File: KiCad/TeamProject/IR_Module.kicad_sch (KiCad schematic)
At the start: 20 parts, among them U1 MCP6294, U4 MCP6294, U4 MCP6546, U6 MCP6294

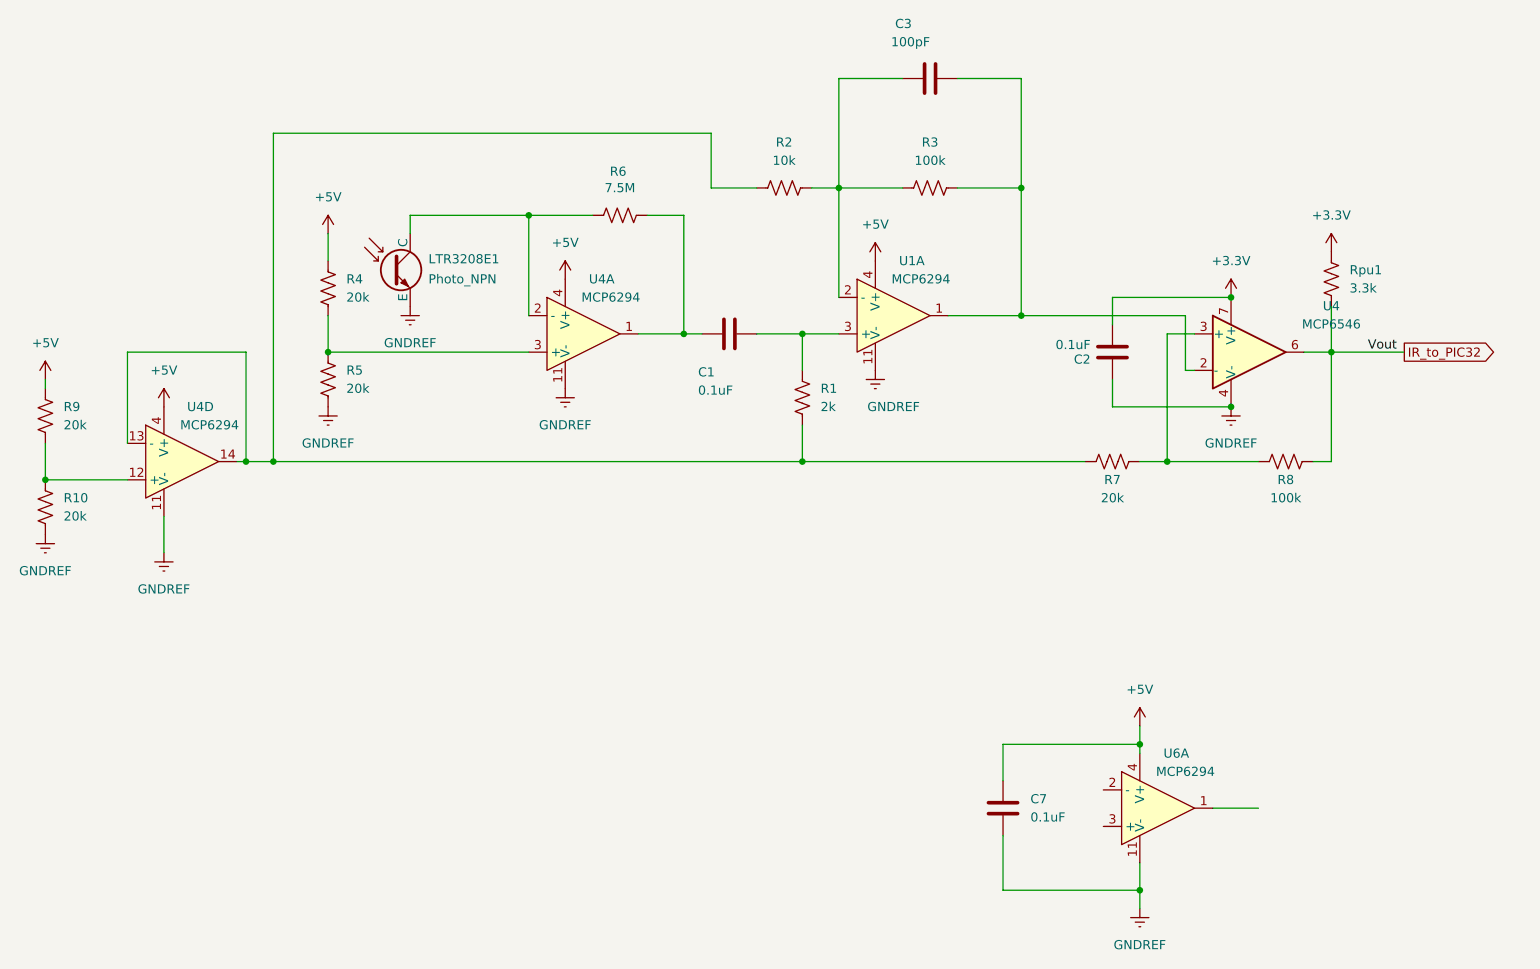
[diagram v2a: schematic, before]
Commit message: Update first-stage amplifier resistor value for IR module
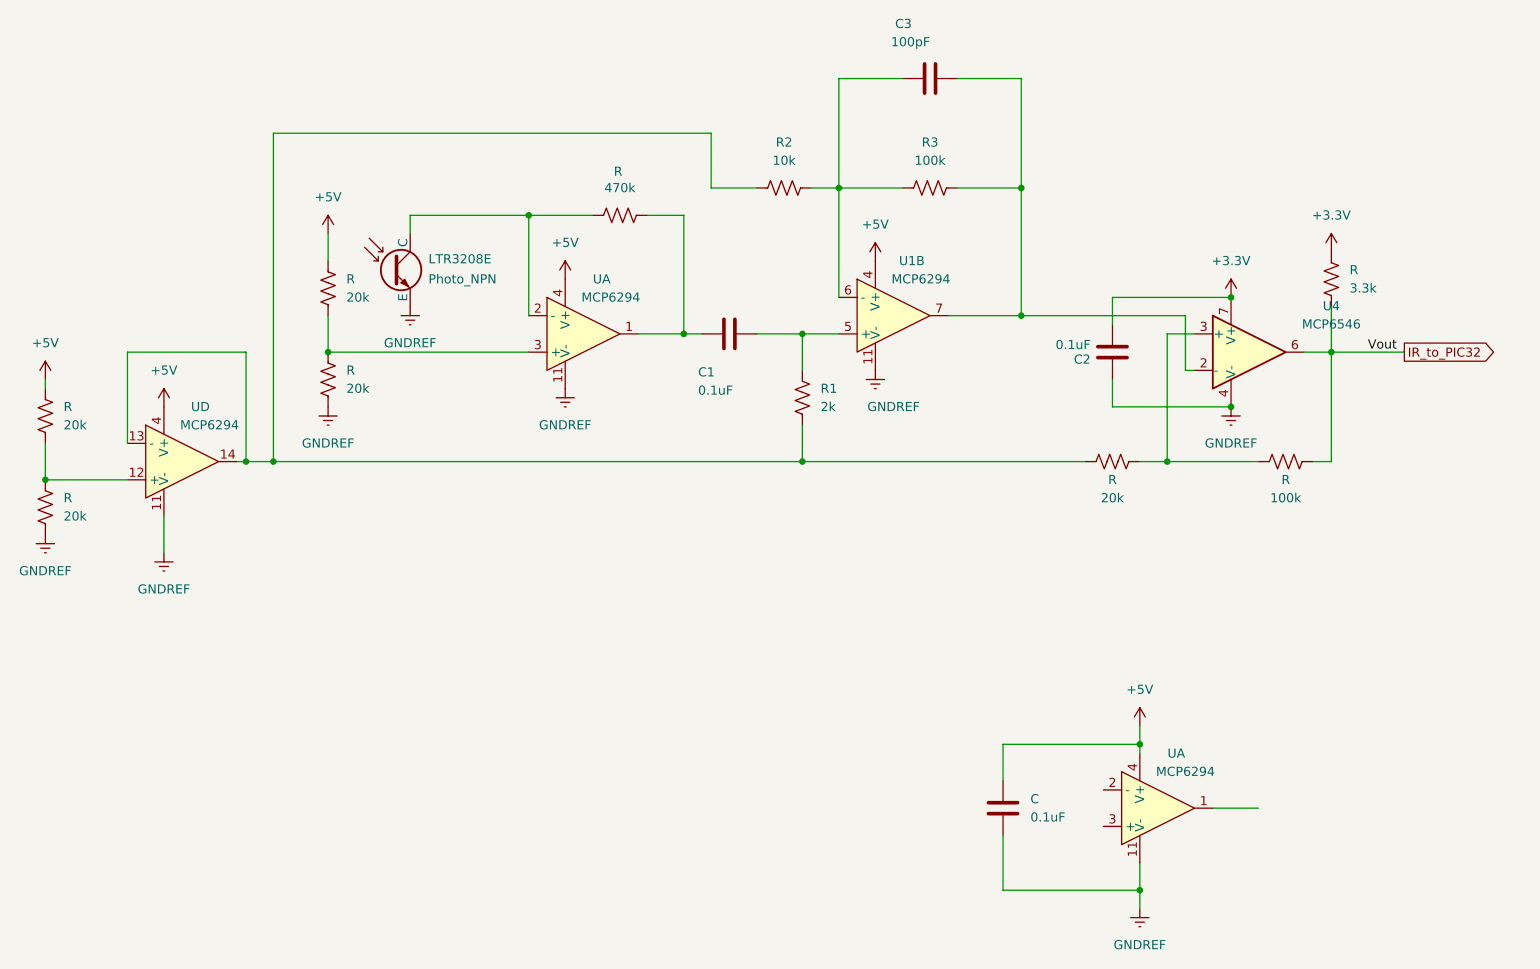
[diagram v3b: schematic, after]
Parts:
- R: renamed from R6; value 7.5M -> 470k
- renumbered C7 to C, LTR3208E1 to LTR3208E, R7 to R, R8 to R, R9 to R, Rpu1 to R, R10 to R, R5 to R, R4 to R, U4 to U, U6 to U
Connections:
- net at C3.1, R3.2, U4.2 (-): now also U1.7; no longer U1.1
- net at C3.2, R2.2, R3.1: now also U1.6 (-); no longer U1.2 (-)
- net at C1.1, R1.2: now also U1.5 (+); no longer U1.3 (+)
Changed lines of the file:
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@@
 		(on_board yes)
 		(dnp no)
-		(property "Reference" "#PWR?"
+		(property "Reference" "#PWR02"
 			(at 166.37 90.17 0)
 			(effects
@@
 		(on_board yes)
 		(dnp no)
-		(property "Reference" "C?"
+		(property "Reference" "C2"
 			(at 196.342 82.296 0)
 			(effects
@@
 		(lib_id "ME218_BaseLib:MCP6294")
 		(at 168.91 76.2 0)
-		(unit 1)
-		(exclude_from_sim no)
-		(in_bom yes)
-		(on_board yes)
-		(dnp no)
-		(property "Reference" "U?"
+		(unit 2)
+		(exclude_from_sim no)
+		(in_bom yes)
+		(on_board yes)
+		(dnp no)
+		(property "Reference" "U1"
 			(at 171.45 68.58 0)
 			(effects
@@
 		(on_board yes)
 		(dnp no)
-		(property "Reference" "R7"
+		(property "Reference" "R"
 			(at 199.39 99.06 90)
 			(effects
@@
 		(dnp no)
 		(fields_autoplaced yes)
-		(property "Reference" "R?"
+		(property "Reference" "R3"
 			(at 173.99 52.07 90)
 			(effects
@@
 		(dnp no)
 		(fields_autoplaced yes)
-		(property "Reference" "R?"
+		(property "Reference" "R1"
 			(at 158.75 86.3599 0)
 			(effects
@@
 		(dnp no)
 		(fields_autoplaced yes)
-		(property "Reference" "#PWR?"
+		(property "Reference" "#PWR03"
 			(at 101.6 81.28 0)
 			(effects
@@
 		(dnp no)
 		(fields_autoplaced yes)
-		(property "Reference" "#PWR09"
+		(property "Reference" "#PWR?"
 			(at 90.17 95.25 0)
 			(effects
@@
 		(on_board yes)
 		(dnp no)
-		(property "Reference" "R8"
+		(property "Reference" "R"
 			(at 223.52 99.06 90)
 			(effects
@@
 		(dnp no)
 		(fields_autoplaced yes)
-		(property "Reference" "R9"
+		(property "Reference" "R"
 			(at 53.34 88.8999 0)
 			(effects
@@
 		(dnp no)
 		(fields_autoplaced yes)
-		(property "Reference" "#PWR?"
+		(property "Reference" "#PWR01"
 			(at 166.37 72.39 0)
 			(effects
@@
 		(on_board yes)
 		(dnp no)
-		(property "Reference" "U?"
+		(property "Reference" "U4"
 			(at 229.87 74.8598 0)
 			(effects
@@
 		(dnp no)
 		(fields_autoplaced yes)
-		(property "Reference" "#PWR029"
+		(property "Reference" "#PWR?"
 			(at 215.9 77.47 0)
 			(effects
@@
 		(dnp no)
 		(fields_autoplaced yes)
-		(property "Reference" "#PWR032"
+		(property "Reference" "#PWR?"
 			(at 67.31 115.57 0)
 			(effects
@@
 		(on_board yes)
 		(dnp no)
-		(property "Reference" "C?"
+		(property "Reference" "C1"
 			(at 144.018 84.074 90)
 			(effects
@@
 		(dnp no)
 		(fields_autoplaced yes)
-		(property "Reference" "#PWR023"
+		(property "Reference" "#PWR?"
 			(at 123.19 74.93 0)
 			(effects
@@
 		(on_board yes)
 		(dnp no)
-		(property "Reference" "C?"
+		(property "Reference" "C3"
 			(at 171.45 35.56 90)
 			(effects
@@
 		(dnp no)
 		(fields_autoplaced yes)
-		(property "Reference" "C7"
+		(property "Reference" "C"
 			(at 187.96 143.5099 0)
 			(effects
@@
 		(dnp no)
 		(fields_autoplaced yes)
-		(property "Reference" "#PWR030"
+		(property "Reference" "#PWR?"
 			(at 215.9 95.25 0)
 			(effects
@@
 		(dnp no)
 		(fields_autoplaced yes)
-		(property "Reference" "#PWR024"
+		(property "Reference" "#PWR?"
 			(at 123.19 92.71 0)
 			(effects
@@
 		(dnp no)
 		(fields_autoplaced yes)
-		(property "Reference" "#PWR021"
+		(property "Reference" "#PWR?"
 			(at 50.8 113.03 0)
 			(effects
@@
 		(dnp no)
 		(fields_autoplaced yes)
-		(property "Reference" "#PWR031"
+		(property "Reference" "#PWR?"
 			(at 67.31 92.71 0)
 			(effects
@@
 		(on_board yes)
 		(dnp no)
-		(property "Reference" "U4"
+		(property "Reference" "U"
 			(at 72.39 88.9 0)
 			(effects
@@
 		(dnp no)
 		(fields_autoplaced yes)
-		(property "Reference" "#PWR020"
+		(property "Reference" "#PWR?"
 			(at 50.8 88.9 0)
 			(effects
@@
 		(dnp no)
 		(fields_autoplaced yes)
-		(property "Reference" "Rpu1"
+		(property "Reference" "R"
 			(at 232.41 69.8499 0)
 			(effects
@@
 		(on_board yes)
 		(dnp no)
-		(property "Reference" "LTR3208E1"
+		(property "Reference" "LTR3208E"
 			(at 104.14 68.326 0)
 			(effects
@@
 		(dnp no)
 		(fields_autoplaced yes)
-		(property "Reference" "R10"
+		(property "Reference" "R"
 			(at 53.34 101.5999 0)
 			(effects
@@
 		(on_board yes)
 		(dnp no)
-		(property "Reference" "R6"
+		(property "Reference" "R"
 			(at 130.556 56.134 90)
 			(effects
@@
 			)
 		)
-		(property "Value" "7.5M"
+		(property "Value" "470k"
 			(at 130.81 58.42 90)
 			(effects
@@
 		(on_board yes)
 		(dnp no)
-		(property "Reference" "U4"
+		(property "Reference" "U"
 			(at 128.27 71.12 0)
 			(effects
@@
 		(dnp no)
 		(fields_autoplaced yes)
-		(property "Reference" "R5"
+		(property "Reference" "R"
 			(at 92.71 83.8199 0)
 			(effects
@@
 		(dnp no)
 		(fields_autoplaced yes)
-		(property "Reference" "#PWR027"
+		(property "Reference" "#PWR?"
 			(at 229.87 71.12 0)
 			(effects
@@
 		(dnp no)
 		(fields_autoplaced yes)
-		(property "Reference" "#PWR025"
+		(property "Reference" "#PWR?"
 			(at 203.2 137.16 0)
 			(effects
@@
 		(dnp no)
 		(fields_autoplaced yes)
-		(property "Reference" "#PWR026"
+		(property "Reference" "#PWR?"
 			(at 203.2 165.1 0)
 			(effects
@@
 		(on_board yes)
 		(dnp no)
-		(property "Reference" "U6"
+		(property "Reference" "U"
 			(at 208.28 137.16 0)
 			(effects
@@
 		(dnp no)
 		(fields_autoplaced yes)
-		(property "Reference" "#PWR08"
+		(property "Reference" "#PWR?"
 			(at 90.17 68.58 0)
 			(effects
@@
 		(dnp no)
 		(fields_autoplaced yes)
-		(property "Reference" "R4"
+		(property "Reference" "R"
 			(at 92.71 71.1199 0)
 			(effects
@@
 		(dnp no)
 		(fields_autoplaced yes)
-		(property "Reference" "R?"
+		(property "Reference" "R2"
 			(at 153.67 52.07 90)
 			(effects

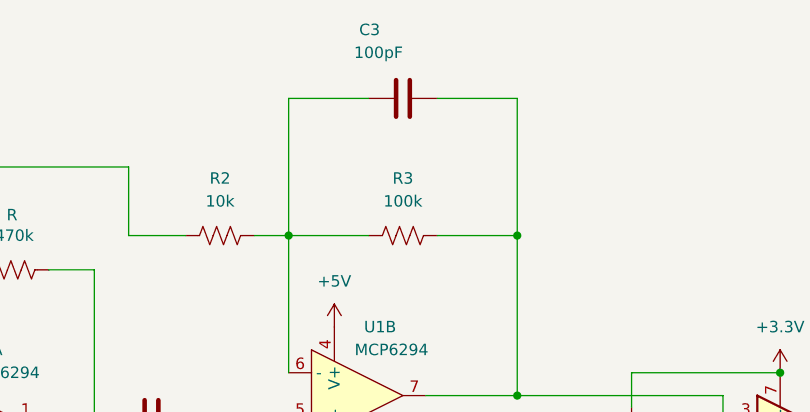
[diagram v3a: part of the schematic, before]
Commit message: Correct definition and capacitor value
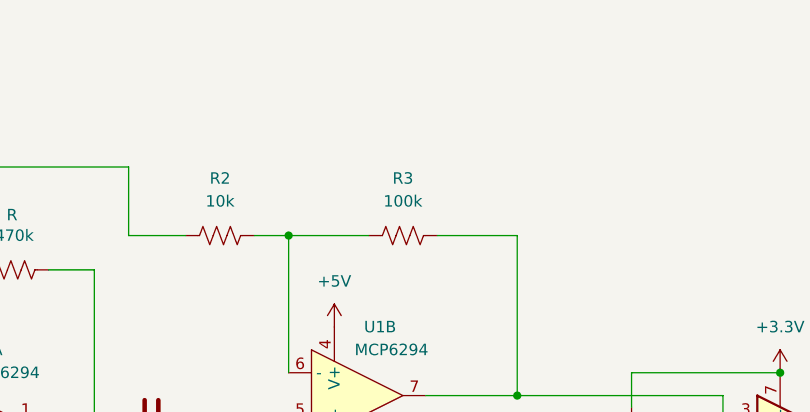
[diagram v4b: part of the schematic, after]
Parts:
- removed C3: 100pF, symbol ME218_BaseLib:Cap
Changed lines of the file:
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@@
 	(paper "A4")
-	(junction
-		(at 186.69 58.42)
-		(diameter 0)
-		(color 0 0 0 0)
-	)
 	(junction
 		(at 215.9 73.66)
@@
 	(wire
 		(pts
-			(xy 170.18 43.18) (xy 161.29 43.18)
-		)
-		(stroke
-			(width 0)
-			(type default)
-		)
-	)
-	(wire
-		(pts
 			(xy 62.23 93.98) (xy 62.23 81.28)
 		)
@@
 	(wire
 		(pts
-			(xy 186.69 43.18) (xy 186.69 58.42)
-		)
-		(stroke
-			(width 0)
-			(type default)
-		)
-	)
-	(wire
-		(pts
 			(xy 203.2 158.75) (xy 203.2 156.21)
 		)
@@
 	(wire
 		(pts
-			(xy 177.8 43.18) (xy 186.69 43.18)
-		)
-		(stroke
-			(width 0)
-			(type default)
-		)
-	)
-	(wire
-		(pts
 			(xy 161.29 58.42) (xy 170.18 58.42)
 		)
@@
 		(pts
 			(xy 199.39 73.66) (xy 215.9 73.66)
-		)
-		(stroke
-			(width 0)
-			(type default)
-		)
-	)
-	(wire
-		(pts
-			(xy 161.29 43.18) (xy 161.29 58.42)
 		)
 		(stroke
@@
 					(unit 1)
 				)
-			)
-		)
-	)
-	(symbol
-		(lib_id "ME218_BaseLib:Cap")
-		(at 173.99 43.18 270)
-		(unit 1)
-		(exclude_from_sim no)
-		(in_bom yes)
-		(on_board yes)
-		(dnp no)
-		(property "Reference" "C3"
-			(at 171.45 35.56 90)
-			(effects
-				(font
-					(size 1.27 1.27)
-				)
-				(justify right)
-			)
-		)
-		(property "Value" "100pF"
-			(at 173.99 38.1 90)
-			(effects
-				(font
-					(size 1.27 1.27)
-				)
-				(justify right)
-			)
-		)
-		(property "Footprint" ""
-			(at 170.18 44.1452 0)
-			(effects
-				(font
-					(size 1.27 1.27)
-				)
-				(hide yes)
-			)
-		)
-		(property "Datasheet" ""
-			(at 173.99 43.18 0)
-			(effects
-				(font
-					(size 1.27 1.27)
-				)
-				(hide yes)
-			)
-		)
-		(property "Description" ""
-			(at 173.99 43.18 0)
-			(effects
-				(font
-					(size 1.27 1.27)
-				)
-			)
-		)
-		(pin "1"
-		)
-		(pin "2"
-		)
-		(instances
-			(project "IR_Module"
-				(path "/5e537725-9b82-46dd-ad10-a39d09eacea6"
-					(reference "C3")
-					(unit 1)
-				)
-			)
-			(project "Leader"
-				(path "/e69a436c-b634-4c28-b262-47742fc47b6f/415f1343-5bea-4de7-9b3a-ad5b76fd5938"
-					(reference "C?")
-					(unit 1)
-				)
